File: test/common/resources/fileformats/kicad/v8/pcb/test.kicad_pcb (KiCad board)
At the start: 2 copper layers, 4 parts

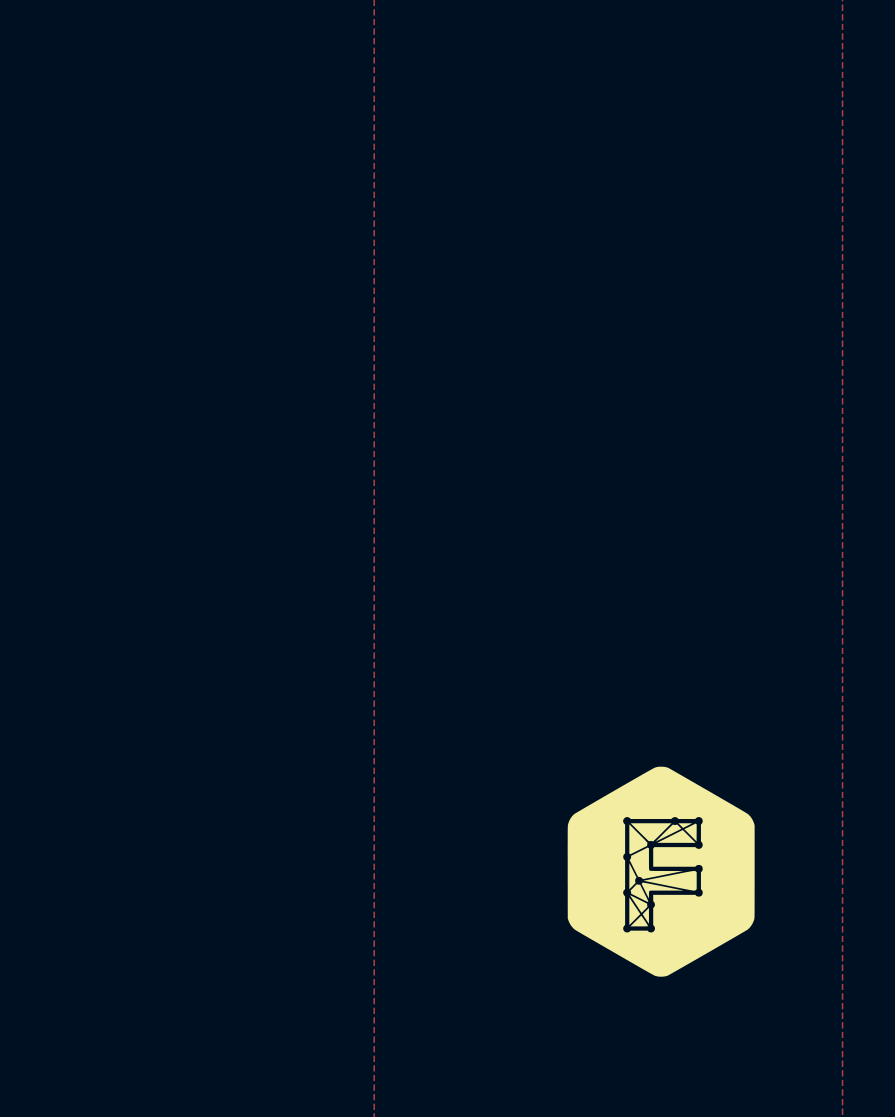
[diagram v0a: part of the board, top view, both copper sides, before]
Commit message: UI: Layout-Viewer: Refactor and improvement (#1707)
<!-- CURSOR_SUMMARY -->
> [!NOTE]
> **Medium Risk**
> Large refactor of the layout editor’s interaction model (selection,
dragging, and action dispatch) plus changes to standalone server
startup, which could introduce UI regressions or mismatched backend
expectations for action/selection payloads.
> 
> **Overview**
> Improves the PCB layout editor UX by adding **group-aware selection**,
**multi-select via Shift+drag box selection**, and richer
hover/selection visuals; move/rotate/flip/undo/redo now operate on the
current selection set (including footprint groups, with double-click
“single override” mode).
> 
> Adds a separate canvas-based **text overlay** to render
footprint/board text and pad annotations, and shifts layer
colors/visibility defaults to be driven by `model.layers` metadata
instead of hardcoded mappings.
> 
> Refactors the standalone layout server entrypoint to a Typer-based CLI
with a `create_app` factory, shared router wiring, static/index serving,
and an automatic frontend bundle build check; also updates `.gitignore`
for layout-editor build artifacts and extends `ato dev install` to
support an `antigravity` IDE target.
> 
> <sup>Written by [Cursor
Bugbot](https://cursor.com/dashboard?tab=bugbot) for commit
c979dc5021cf381ac183a3e334a8e41b00bc5921. This will update automatically
on new commits. Configure
[here](https://cursor.com/dashboard?tab=bugbot).</sup>
<!-- /CURSOR_SUMMARY -->

---------

Co-authored-by: Claude Opus 4.6 <noreply@anthropic.com>
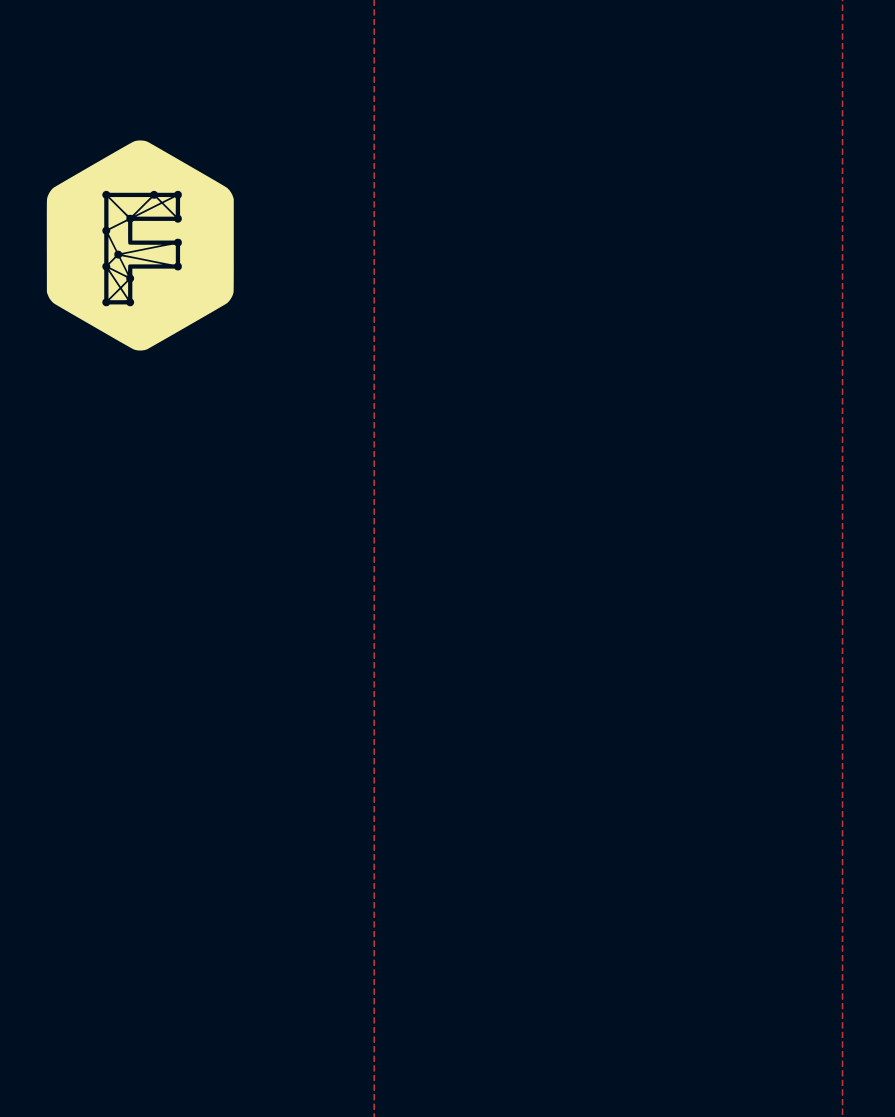
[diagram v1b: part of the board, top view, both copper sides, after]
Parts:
- moved G*** 34.8 mm to (10.0, 20.0)
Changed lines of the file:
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@@
 			(usegerberadvancedattributes yes)
 			(creategerberjobfile yes)
-			(dashed_line_dash_ratio 12.000000)
-			(dashed_line_gap_ratio 3.000000)
+			(dashed_line_dash_ratio 12)
+			(dashed_line_gap_ratio 3)
 			(svgprecision 4)
 			(plotframeref no)
@@
 			(hpglpennumber 1)
 			(hpglpenspeed 20)
-			(hpglpendiameter 15.000000)
+			(hpglpendiameter 15)
 			(pdf_front_fp_property_popups yes)
 			(pdf_back_fp_property_popups yes)
@@
 			(psnegative no)
 			(psa4output no)
+			(plotinvisibletext no)
+			(sketchpadsonfab no)
 			(plotreference yes)
 			(plotvalue yes)
 			(plotfptext yes)
-			(plotinvisibletext no)
-			(sketchpadsonfab no)
 			(subtractmaskfromsilk no)
 			(outputformat 1)
@@
 	(footprint "logos:faebryk_logo"
 		(layer "F.Cu")
-		(at 32.25 46.75)
+		(at 10 20 0)
 		(property "Reference" "G***"
 			(at 0 0 0)
@@
 				)
 				(justify mirror right)
-				(justify bottom)
 			)
 		)
